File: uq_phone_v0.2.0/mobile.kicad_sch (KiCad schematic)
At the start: 25 parts, among them J10 513382474, J11 513382474, J4 20279-001E-03, J5 20279-001E-03, U4 WP SNAP-IN BASE_6000636

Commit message: Another day of routing and adding components
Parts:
- removed C13: 47uF, Capacitor_SMD:C_0805_2012Metric, symbol Capacitors:Capacitor_47uF
- added C13, C27, C52, C53: 220uF, Capacitor_SMD:C_1206_3216Metric, symbol Capacitors:Capacitor_220uF
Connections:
- net GND: now also C13.2, C27.2, C52.2, C53.2
- net VBAT: now also C13.1, C27.1, C52.1, C53.1
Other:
- moved on the sheet: TP17, U4C

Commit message: Restructure, route and add flex pcb
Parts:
- C10, C11, C12, C13, C27, C52, C53, C8, C9, J10, J11, J4, J5, R12, R13, R14, R15, TP10, TP11, TP12, TP13, TP14, TP15, TP16, TP17, TP8, TP9, U4: now left out of the parts list
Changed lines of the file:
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@@
 		(unit 1)
 		(exclude_from_sim no)
-		(in_bom yes)
+		(in_bom no)
 		(on_board no)
 		(dnp no)
@@
 		(unit 2)
 		(exclude_from_sim no)
-		(in_bom yes)
+		(in_bom no)
 		(on_board no)
 		(dnp no)
@@
 		(unit 3)
 		(exclude_from_sim no)
-		(in_bom yes)
+		(in_bom no)
 		(on_board no)
 		(dnp no)
@@
 		(unit 1)
 		(exclude_from_sim no)
-		(in_bom yes)
+		(in_bom no)
 		(on_board no)
 		(dnp no)
@@
 		(unit 1)
 		(exclude_from_sim no)
-		(in_bom yes)
+		(in_bom no)
 		(on_board no)
 		(dnp no)
@@
 		(unit 1)
 		(exclude_from_sim no)
-		(in_bom yes)
+		(in_bom no)
 		(on_board no)
 		(dnp no)
@@
 		(unit 1)
 		(exclude_from_sim no)
-		(in_bom yes)
+		(in_bom no)
 		(on_board no)
 		(dnp no)
@@
 		(unit 1)
 		(exclude_from_sim no)
-		(in_bom yes)
+		(in_bom no)
 		(on_board no)
 		(dnp no)
@@
 		(unit 1)
 		(exclude_from_sim no)
-		(in_bom yes)
+		(in_bom no)
 		(on_board no)
 		(dnp no)
@@
 		(unit 1)
 		(exclude_from_sim no)
-		(in_bom yes)
+		(in_bom no)
 		(on_board no)
 		(dnp no)
@@
 		(unit 1)
 		(exclude_from_sim no)
-		(in_bom yes)
+		(in_bom no)
 		(on_board no)
 		(dnp no)
@@
 		(unit 1)
 		(exclude_from_sim no)
-		(in_bom yes)
+		(in_bom no)
 		(on_board no)
 		(dnp no)
@@
 		(unit 1)
 		(exclude_from_sim no)
-		(in_bom yes)
+		(in_bom no)
 		(on_board no)
 		(dnp no)
@@
 		(unit 1)
 		(exclude_from_sim no)
-		(in_bom yes)
+		(in_bom no)
 		(on_board no)
 		(dnp no)
@@
 		(unit 1)
 		(exclude_from_sim no)
-		(in_bom yes)
+		(in_bom no)
 		(on_board no)
 		(dnp no)
@@
 		(unit 1)
 		(exclude_from_sim no)
-		(in_bom yes)
+		(in_bom no)
 		(on_board no)
 		(dnp no)
@@
 		(unit 1)
 		(exclude_from_sim no)
-		(in_bom yes)
+		(in_bom no)
 		(on_board no)
 		(dnp no)
@@
 		(unit 1)
 		(exclude_from_sim no)
-		(in_bom yes)
+		(in_bom no)
 		(on_board no)
 		(dnp no)
@@
 		(unit 1)
 		(exclude_from_sim no)
-		(in_bom yes)
+		(in_bom no)
 		(on_board no)
 		(dnp no)
@@
 		(unit 1)
 		(exclude_from_sim no)
-		(in_bom yes)
+		(in_bom no)
 		(on_board no)
 		(dnp no)
@@
 		(unit 1)
 		(exclude_from_sim no)
-		(in_bom yes)
+		(in_bom no)
 		(on_board no)
 		(dnp no)
@@
 		(unit 1)
 		(exclude_from_sim no)
-		(in_bom yes)
+		(in_bom no)
 		(on_board no)
 		(dnp no)
@@
 		(unit 1)
 		(exclude_from_sim no)
-		(in_bom yes)
+		(in_bom no)
 		(on_board no)
 		(dnp no)
@@
 		(unit 1)
 		(exclude_from_sim no)
-		(in_bom yes)
+		(in_bom no)
 		(on_board no)
 		(dnp no)
@@
 		(unit 1)
 		(exclude_from_sim no)
-		(in_bom yes)
+		(in_bom no)
 		(on_board no)
 		(dnp no)
@@
 		(unit 1)
 		(exclude_from_sim no)
-		(in_bom yes)
+		(in_bom no)
 		(on_board no)
 		(dnp no)
@@
 		(unit 1)
 		(exclude_from_sim no)
-		(in_bom yes)
+		(in_bom no)
 		(on_board no)
 		(dnp no)
@@
 		(unit 1)
 		(exclude_from_sim no)
-		(in_bom yes)
+		(in_bom no)
 		(on_board no)
 		(dnp no)
@@
 		(unit 1)
 		(exclude_from_sim no)
-		(in_bom yes)
+		(in_bom no)
 		(on_board no)
 		(dnp no)
@@
 		(unit 1)
 		(exclude_from_sim no)
-		(in_bom yes)
+		(in_bom no)
 		(on_board no)
 		(dnp no)
@@
 		(unit 1)
 		(exclude_from_sim no)
-		(in_bom yes)
+		(in_bom no)
 		(on_board no)
 		(dnp no)
@@
 		(unit 1)
 		(exclude_from_sim no)
-		(in_bom yes)
+		(in_bom no)
 		(on_board no)
 		(dnp no)
@@
 		(unit 1)
 		(exclude_from_sim no)
-		(in_bom yes)
+		(in_bom no)
 		(on_board no)
 		(dnp no)
@@
 		(unit 1)
 		(exclude_from_sim no)
-		(in_bom yes)
+		(in_bom no)
 		(on_board no)
 		(dnp no)
@@
 		(unit 1)
 		(exclude_from_sim no)
-		(in_bom yes)
+		(in_bom no)
 		(on_board no)
 		(dnp no)
@@
 		(unit 1)
 		(exclude_from_sim no)
-		(in_bom yes)
+		(in_bom no)
 		(on_board no)
 		(dnp no)
@@
 		(unit 1)
 		(exclude_from_sim no)
-		(in_bom yes)
+		(in_bom no)
 		(on_board no)
 		(dnp no)
@@
 		(unit 1)
 		(exclude_from_sim no)
-		(in_bom yes)
+		(in_bom no)
 		(on_board no)
 		(dnp no)
@@
 		(unit 1)
 		(exclude_from_sim no)
-		(in_bom yes)
+		(in_bom no)
 		(on_board no)
 		(dnp no)
@@
 		(unit 1)
 		(exclude_from_sim no)
-		(in_bom yes)
+		(in_bom no)
 		(on_board no)
 		(dnp no)
@@
 		(unit 1)
 		(exclude_from_sim no)
-		(in_bom yes)
+		(in_bom no)
 		(on_board no)
 		(dnp no)
@@
 		(unit 1)
 		(exclude_from_sim no)
-		(in_bom yes)
+		(in_bom no)
 		(on_board no)
 		(dnp no)

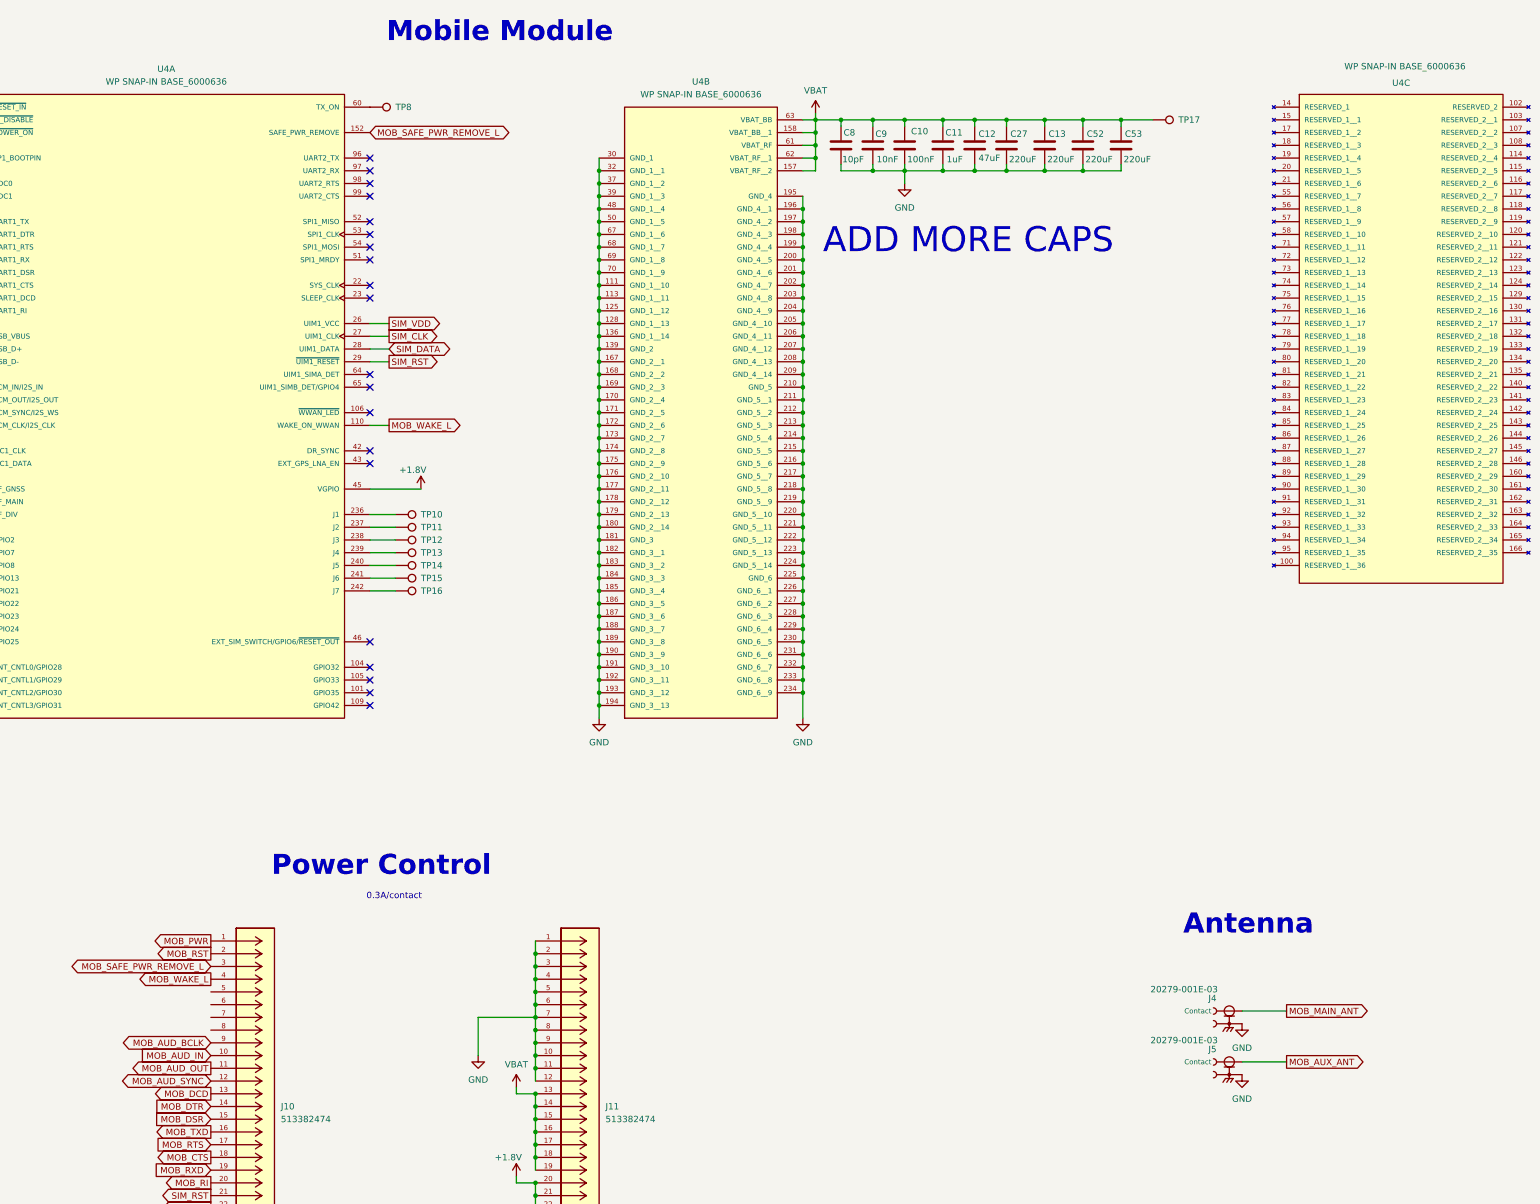
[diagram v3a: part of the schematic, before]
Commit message: New logic level shifters
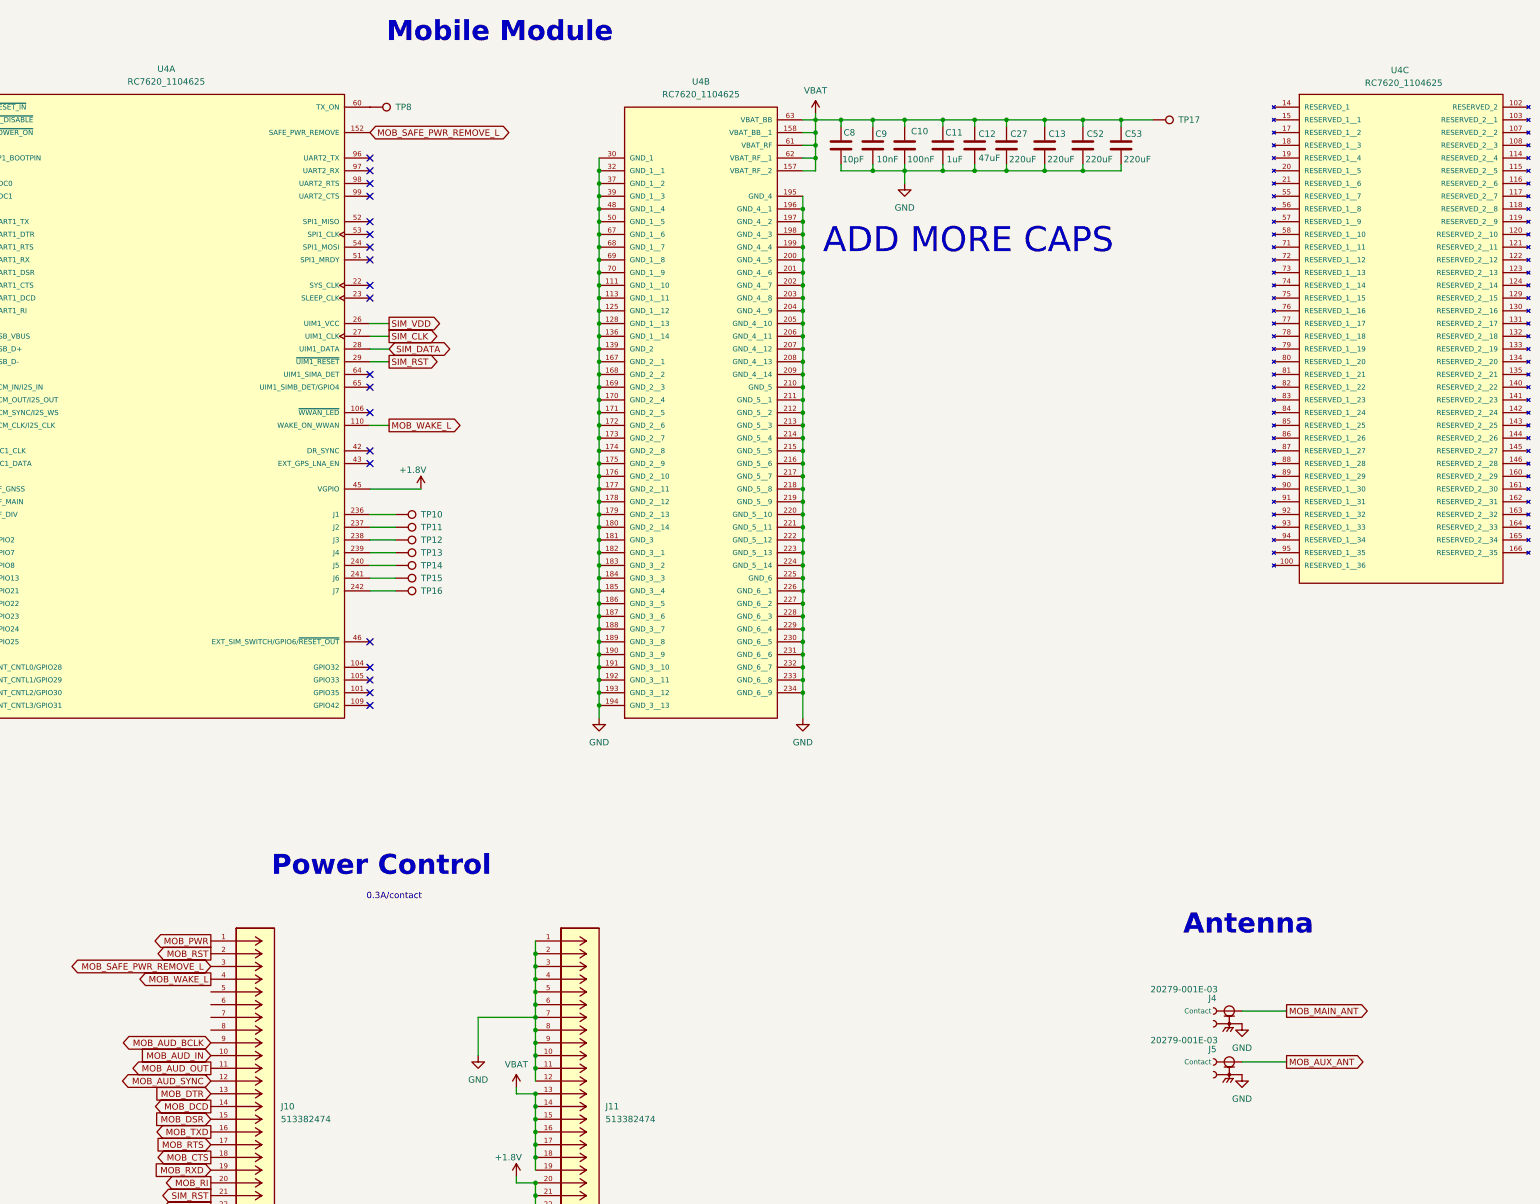
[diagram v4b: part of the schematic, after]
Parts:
- U4: value WP SNAP-IN BASE_6000636 -> RC7620_1104625
- U4: value WP SNAP-IN BASE_6000636 -> RC7620_1104625; footprint WP_SNAP-IN_BASE:SIERRA_WP_SNAP-IN_BASE -> RC7620_1104625:XCVR_RC7620_1104625
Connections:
- net MOB_DCD: now also J10.14; no longer J10.13
- net MOB_DTR: now also J10.13; no longer J10.14

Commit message: Add GNSS antenna for sag
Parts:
- added J12: 20279-001E-03, 20279-001E-03:IPEX_20279-001E-03, symbol 20279-001E-03:20279-001E-03
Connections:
- net GND: now also J12.2
- net MOB_GNSS_ANT: now reaches U4.38 (RF_GNSS)
- net MOB_GNSS_ANT: now also J12.1 (Contact)
- no-connect marks 42 -> 41

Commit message: Fixed display pinout
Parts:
- U4: value RC7620_1104625 -> RC7620_1104626
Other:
- note removed: "ADD MORE CAPS"
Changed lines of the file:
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@@
 		)
 	)
-	(text "ADD MORE CAPS"
-		(exclude_from_sim no)
-		(at 283.21 62.23 0)
-		(effects
-			(font
-				(size 5 5)
-			)
-		)
-	)
 	(text "0.3A/contact"
 		(exclude_from_sim no)
@@
 			)
 		)
-		(property "Value" "RC7620_1104625"
+		(property "Value" "RC7620_1104626"
 			(at 229.87 33.02 0)
 			(effects
@@
 			)
 		)
-		(property "Value" "RC7620_1104625"
+		(property "Value" "RC7620_1104626"
 			(at 370.078 30.734 0)
 			(effects
@@
 			)
 		)
-		(property "Value" "RC7620_1104625"
+		(property "Value" "RC7620_1104626"
 			(at 123.19 30.48 0)
 			(effects

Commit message: Cleaning up adn fixing massive mistake
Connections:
- net GND: now also J10.5, J10.6, J10.7, J10.8
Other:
- note added: "UQ Phone"
- note removed: "0.3A/contact"
- note removed: "Antenna"
- note removed: "Mobile Module"
- note removed: "Power Control"
- title: UQ Phone -> Mobile System
- moved on the sheet: J10, J11, J12, J4, J5

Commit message: minor comments
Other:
- note added: "UART Labels in terms of MCU"
- note removed: "MOBILE TX AND RX ARE IN TERMS OF THE MCU FOR WHATEVER REASON MEANING TX->TX & RX->RX"
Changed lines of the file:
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@@
 		)
 	)
-	(text "MOBILE TX AND RX ARE IN TERMS OF THE \nMCU FOR WHATEVER REASON \nMEANING TX->TX & RX->RX"
+	(text "UART Labels in terms of MCU"
 		(exclude_from_sim no)
-		(at 48.514 50.038 0)
+		(at 58.928 54.356 0)
 		(effects
 			(font
